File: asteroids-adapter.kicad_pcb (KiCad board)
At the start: 2 copper layers, 71.3 x 107.7 mm, 16 parts, among them J1 Asteroids PCB connector, J2 Asteroids harness connector, U1 TL074

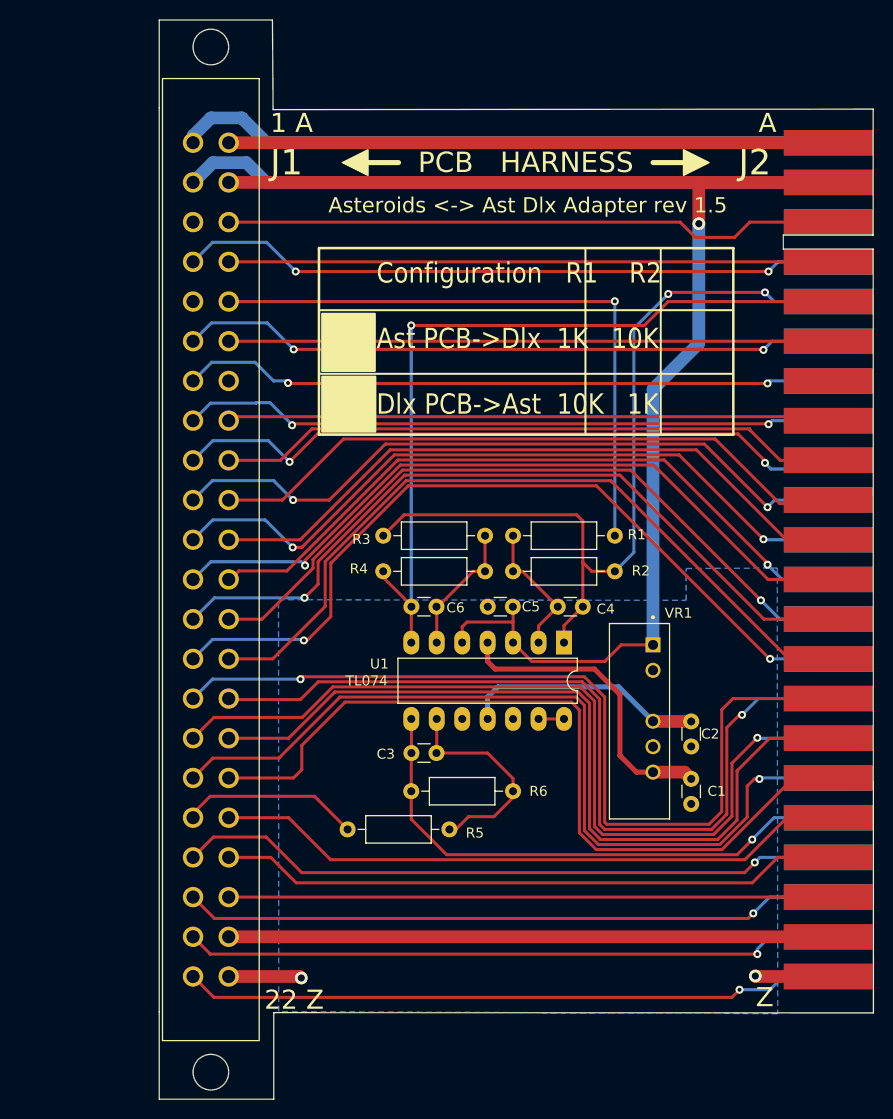
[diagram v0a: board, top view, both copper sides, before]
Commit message: Add jumper for configuration
Configure unused opamp as 0.1x gain, and add jumper to select between
10x and 0.1x gain audio.
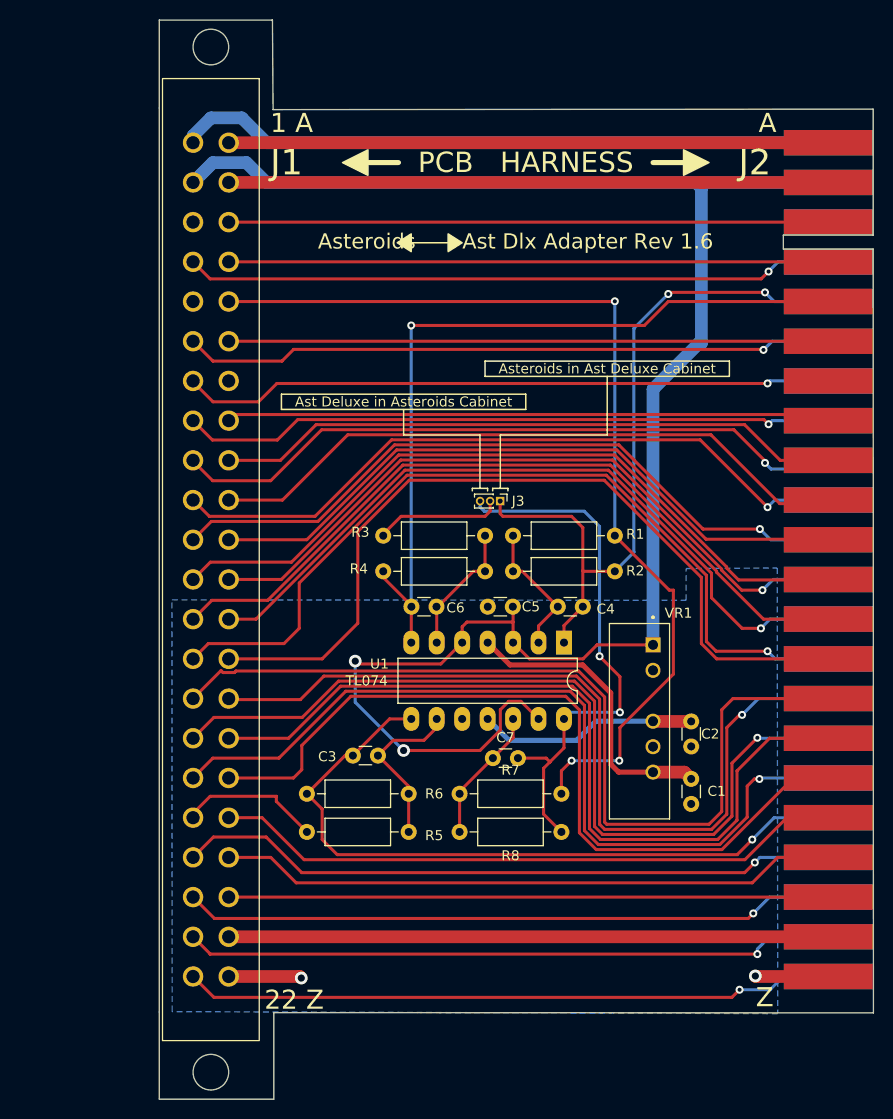
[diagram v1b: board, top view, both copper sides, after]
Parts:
- added C7: Kemet MLCC 100 pF 5% 25V TH, Capacitor_THT:C_Disc_D3.0mm_W1.6mm_P2.50mm, F.Cu at (138.2, 117.3)
- added J3: Conn_01x03, Connector_PinHeader_1.00mm:PinHeader_1x03_P1.00mm_Vertical, F.Cu at (138.9, 91.7)
- added R7: Yageo 10K ohm 1% thin film TH, Resistor_THT:R_Axial_DIN0207_L6.3mm_D2.5mm_P10.16mm_Horizontal, F.Cu at (134.9, 120.9)
- added R8: Yageo 1K ohm 1% thin film TH, Resistor_THT:R_Axial_DIN0207_L6.3mm_D2.5mm_P10.16mm_Horizontal, F.Cu at (145.0, 124.7)
- moved R6 10.4 mm to (119.6, 120.9)
- moved R3 10.2 mm to (127.3, 95.1), turned to 0 degrees
- moved C3 5.85 mm to (126.7, 117.1)
- moved R5 4.07 mm to (129.8, 124.7)
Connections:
- J1 pad 2: VCC -> +5V
- J1 pad B: +5V -> VCC
- J2 pad 2: VCC -> +5V
- J2 pad B: +5V -> VCC
- R3 pad 1: Net-(C6-Pad1) -> Net-(R3-Pad1)
- R3 pad 2: Audio_1_out -> Net-(C6-Pad1)
- U1 pad 12: GND -> Net-(U1-Pad12)
- U1 pad 13: Net-(U1-Pad13) -> +5V
- U1 pad 14: Net-(U1-Pad13) -> Net-(U1-Pad14)
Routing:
- net Net-(U1-Pad14): track 0.00 -> 54.8 mm, vias 0 -> 2
- net +5V: track 133.7 -> 179.2 mm, vias 1 -> 2
- net Audio_2_in: track 61.8 -> 97.6 mm, vias 1 -> 3
- net Y_INV: track 54.6 -> 71.4 mm
- net Net-(U1-Pad12): track 0.00 -> 13.5 mm
- net Net-(R3-Pad1): track 0.00 -> 12.8 mm
- net Audio_1_out: track 83.8 -> 71.9 mm
- net Net-(J1-PadR): track 77.0 -> 83.7 mm
- net VCC: track 65.0 -> 59.7 mm
- net Net-(C3-Pad1): track 21.7 -> 16.8 mm
- net Net-(J1-Pad14): track 80.9 -> 85.1 mm, vias 2 -> 1
- net Y_ORIG: track 17.9 -> 14.3 mm
- net Net-(U1-Pad13): track 2.54 -> 0.00 mm
- net -15V: track 24.4 -> 22.0 mm
- net COIN_SW2: track 72.5 -> 74.4 mm
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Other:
- board text added: "Ast Deluxe in Asteroids Cabinet"
- board text added: "Asteroids Ast Dlx Adapter Rev ${REVISION}"
- board text added: "Asteroids in Ast Deluxe Cabinet"
- board text removed: "Asteroids <-> Ast Dlx Adapter rev 1.5"
- board text removed: "Configuration R1 R2 Ast PCB->Dlx 1K 10K Dlx PCB->Ast 10K 1K"

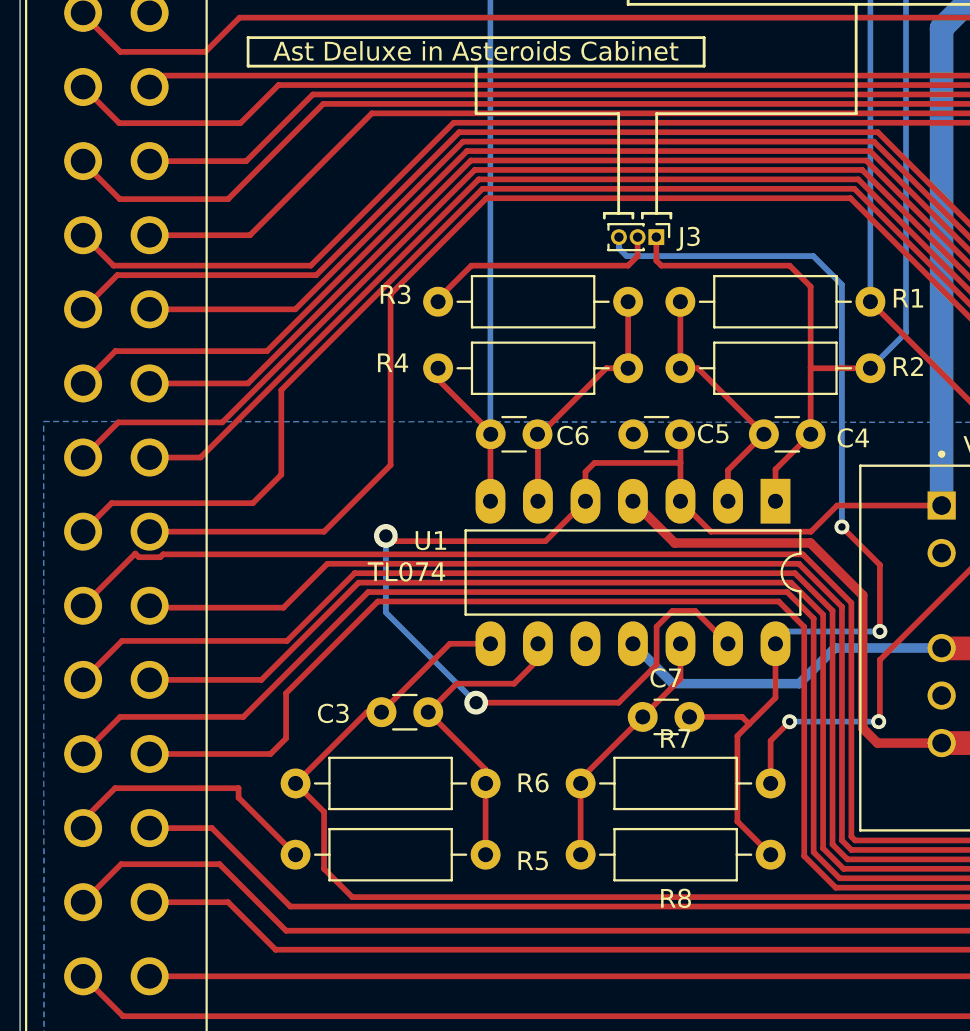
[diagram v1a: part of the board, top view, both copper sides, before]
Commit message: Fixed jumper to 0.1" 3-pin header
also silk screen fixed
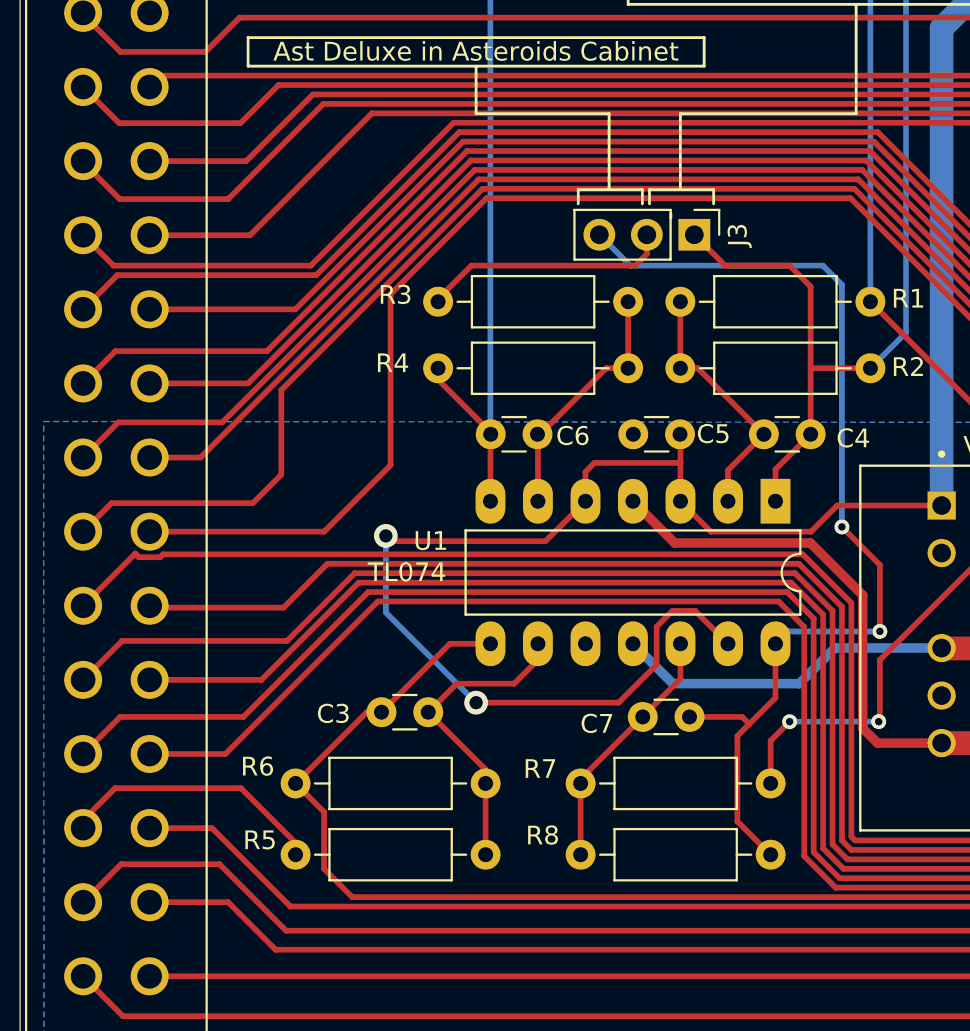
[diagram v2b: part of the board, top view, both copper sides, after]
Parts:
- J3: footprint Connector_PinHeader_1.00mm:PinHeader_1x03_P1.00mm_Vertical -> Connector_PinHeader_2.54mm:PinHeader_1x03_P2.54mm_Vertical
- moved J3 2.04 mm to (141.0, 91.6)
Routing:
- net Audio_1_out: track 71.9 -> 69.1 mm
- net Net-(J1-PadU): track 81.0 -> 79.5 mm
- net Net-(U1-Pad14): track 54.8 -> 55.5 mm
- net Net-(R3-Pad1): track 12.8 -> 13.3 mm

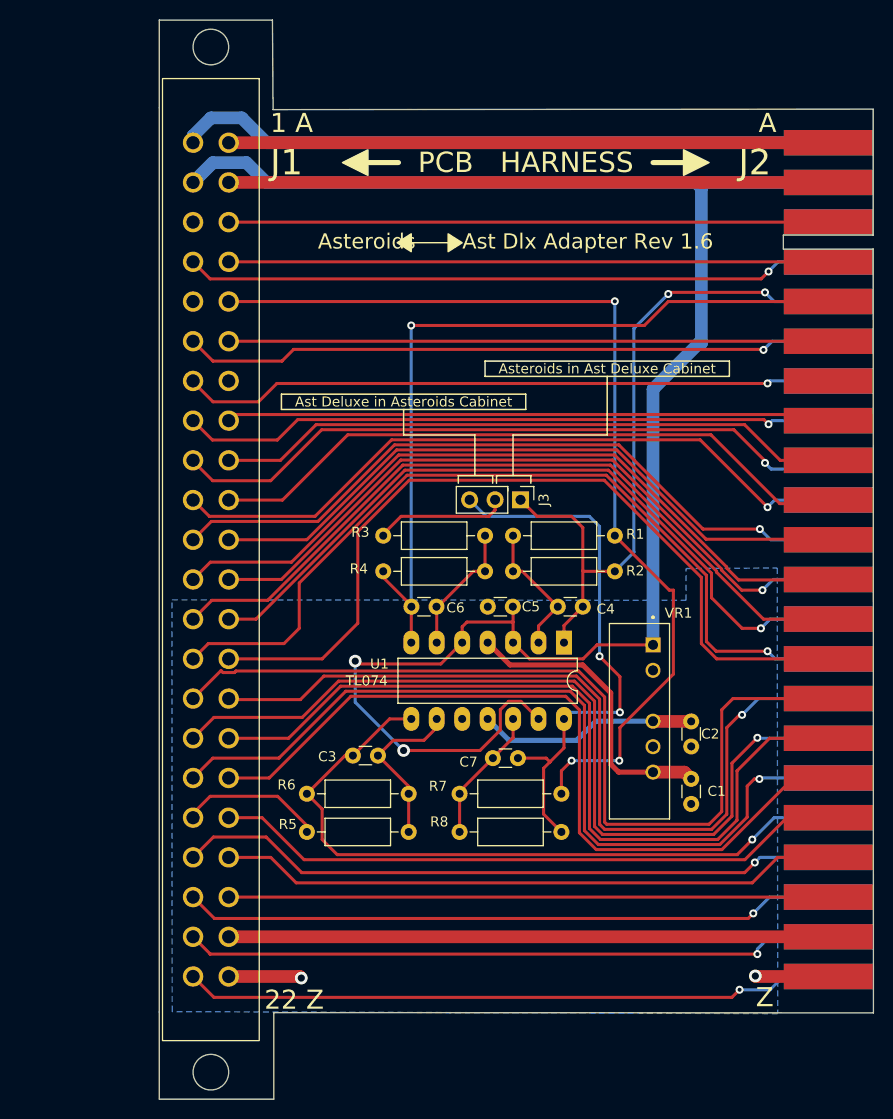
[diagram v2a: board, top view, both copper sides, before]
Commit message: Fixed audio output selection
Audio 1 was always connected to the x10 gain amplifier, instead of the
gain selected by the jumper.

Also, fixed the 3-pin header in the schematic to use the correct 2.54mm
pitch part.
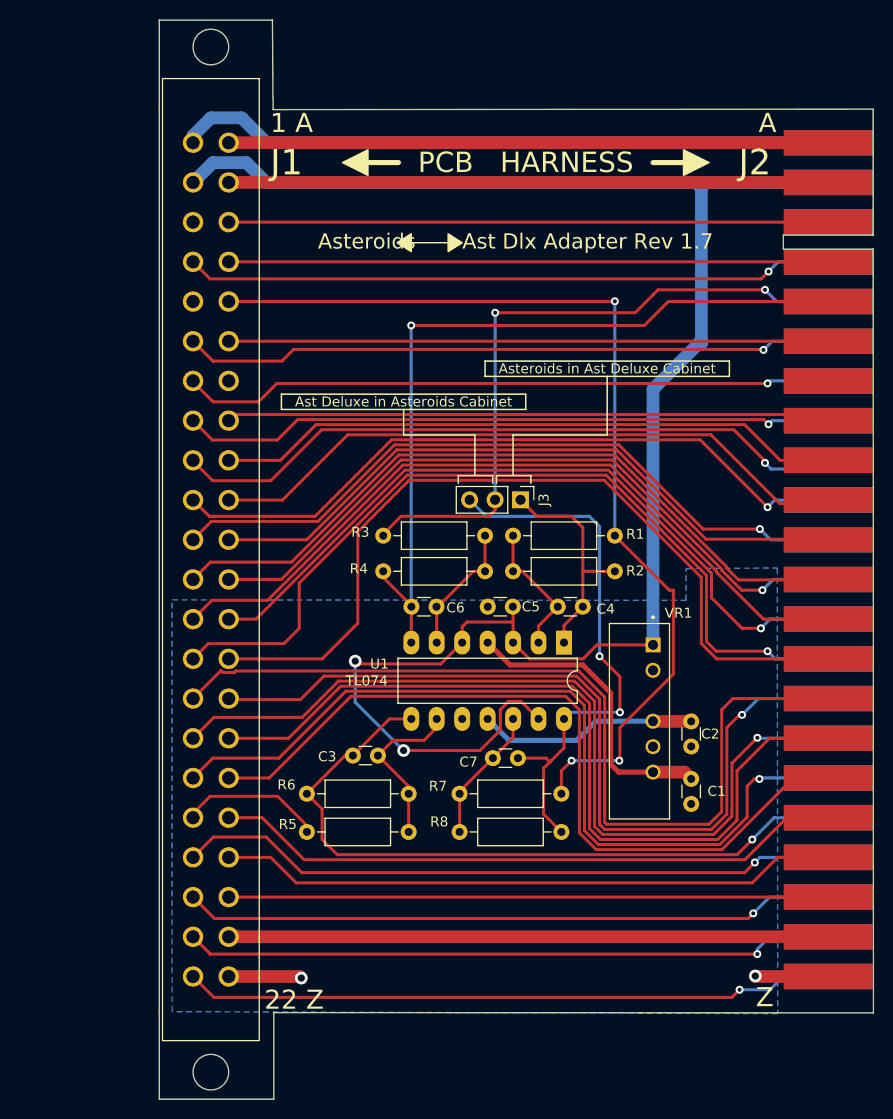
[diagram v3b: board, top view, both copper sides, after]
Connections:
- C4 pad 2: Audio_1_out -> Net-(C4-Pad2)
- J3 pad 1: Audio_1_out -> Net-(C4-Pad2)
- J3 pad 2: Net-(R3-Pad1) -> Audio_1_out
- R2 pad 1: Audio_1_out -> Net-(C4-Pad2)
- R3 pad 1: Net-(R3-Pad1) -> Audio_1_out
- U1 pad 1: Audio_1_out -> Net-(C4-Pad2)
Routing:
- net Net-(C4-Pad2): track 0.00 -> 22.8 mm
- net Net-(R3-Pad1): track 13.3 -> 0.00 mm
- net Net-(J1-PadV): track 63.2 -> 59.0 mm
- net Net-(J1-PadU): track 79.5 -> 76.1 mm
- net Audio_1_out: track 69.1 -> 66.5 mm
- net Net-(J1-PadJ): track 60.2 -> 58.6 mm
- net Net-(J1-Pad9): track 68.5 -> 67.2 mm
- net Y_ORIG: track 14.3 -> 13.3 mm
- net Net-(C3-Pad1): track 16.8 -> 15.9 mm
- net Audio_2_out: track 79.0 -> 78.2 mm
- net Net-(J1-PadL): track 65.4 -> 64.9 mm

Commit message: Universal connector
Update connector footprint to accommodate 0.2 and 0.156 row spacing, and
vertical or right-angle connectors.

Update more parts with full parameters

Add 1M resistor to pin 2 of jumper, so op-amp input isn't floating if
jumper is left out.
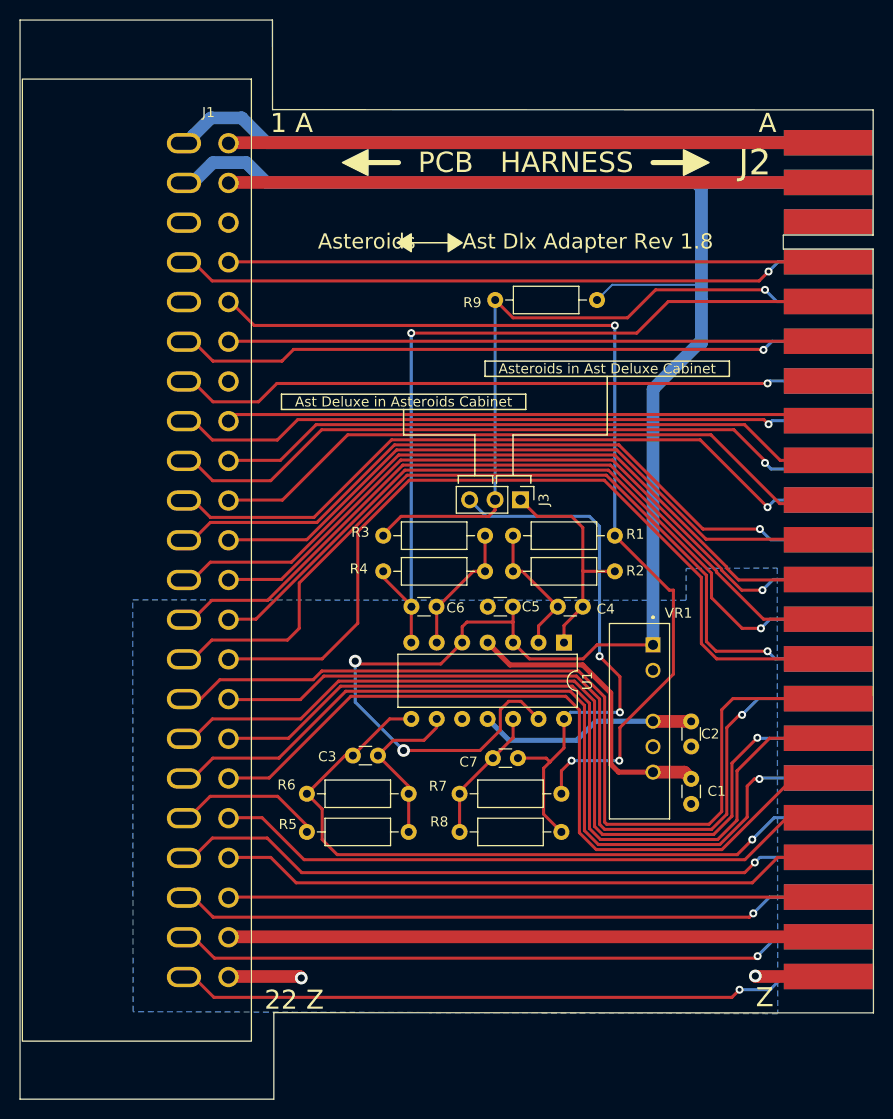
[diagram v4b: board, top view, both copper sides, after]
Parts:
- added R9: Yageo 1Mohm 1% thin film TH_1, Resistor_THT:R_Axial_DIN0207_L6.3mm_D2.5mm_P10.16mm_Horizontal, F.Cu at (148.6, 71.6)
- J1: footprint asteroids-adapter:EDAC-305 44-pin edge 0.156 -> asteroids-adapter: EDAC 44-pin edge 0.156 universal
- U1: footprint Package_DIP:DIP-14_W7.62mm_LongPads -> Package_DIP:DIP-14_W7.62mm
- moved J1 0.78 mm to (109.3, 97.6)
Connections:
- J1 pad C: Net-(J1-PadC) -> unconnected-(J1-PadC)
- J2 pad C: Net-(J1-PadC) -> unconnected-(J2-PadC)
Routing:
- net Net-(J1-PadC): track 59.7 -> 0.00 mm
- net +5V: track 179.2 -> 190.2 mm
- net Audio_1_out: track 66.5 -> 68.8 mm, vias 2 -> 1
- net Audio_2_in: track 97.6 -> 96.2 mm
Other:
- board size 71.3 x 107.7 mm -> 85.2 x 107.7 mm

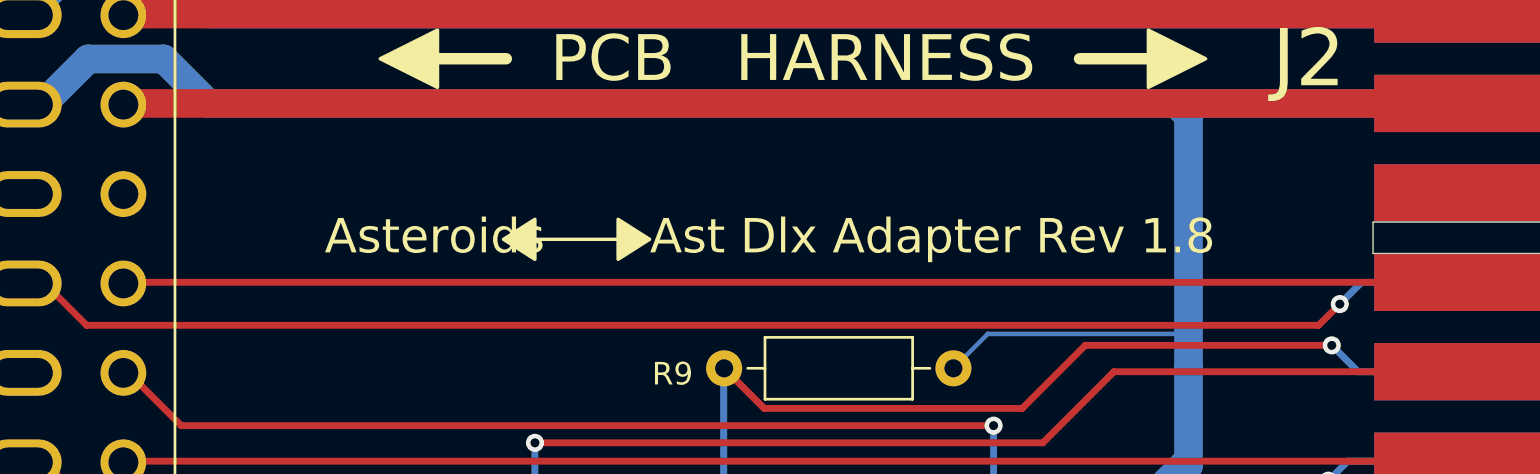
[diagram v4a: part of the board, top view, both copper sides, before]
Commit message: Clean up Makefiles and BOM generation
- Makefiles auto-generate README files

- Fix part parameters and BOM configuration
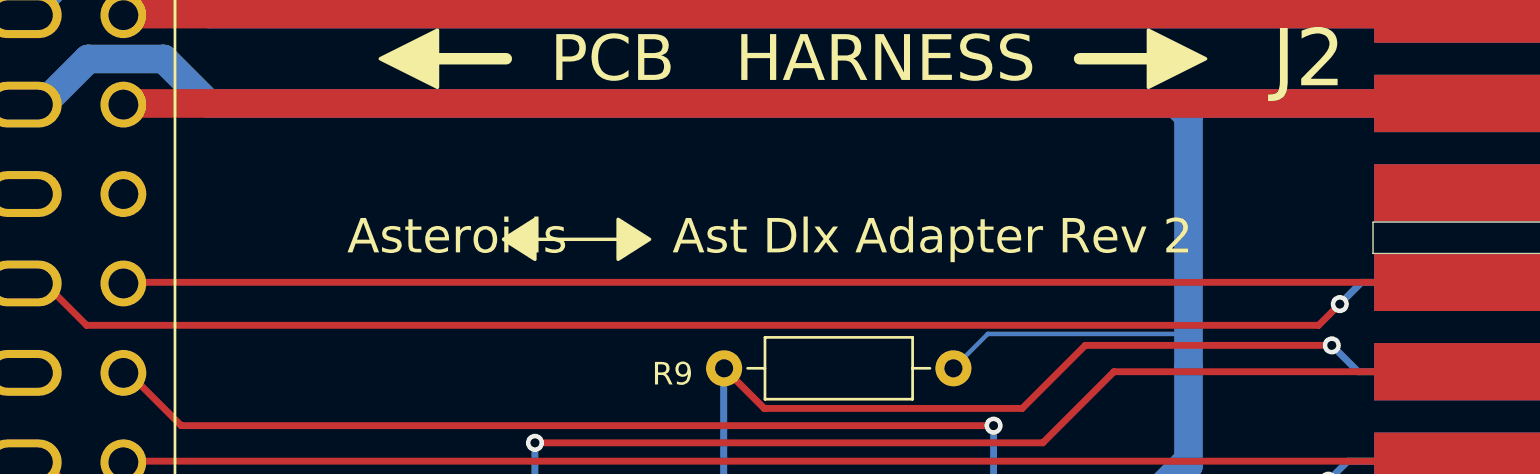
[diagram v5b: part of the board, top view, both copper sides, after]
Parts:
- J3: value Conn_01x03 -> Audio Gain

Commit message: Updated component fields in PCB
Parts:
- J1: value Asteroids PCB connector -> Asteroids Connector EDAC 307-044-558-201 44-pin edge connector, 0.156" right angle
